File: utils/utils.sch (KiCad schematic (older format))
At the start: 20 parts, among them J1 AIN, J2 BIN, J3 GATE, J4 EURORACK_CONN_16, J5 ~OUT, J6 OUT, U1 TL072, U2 4066, U3 LM317L_TO92, U4 LM337L_TO92

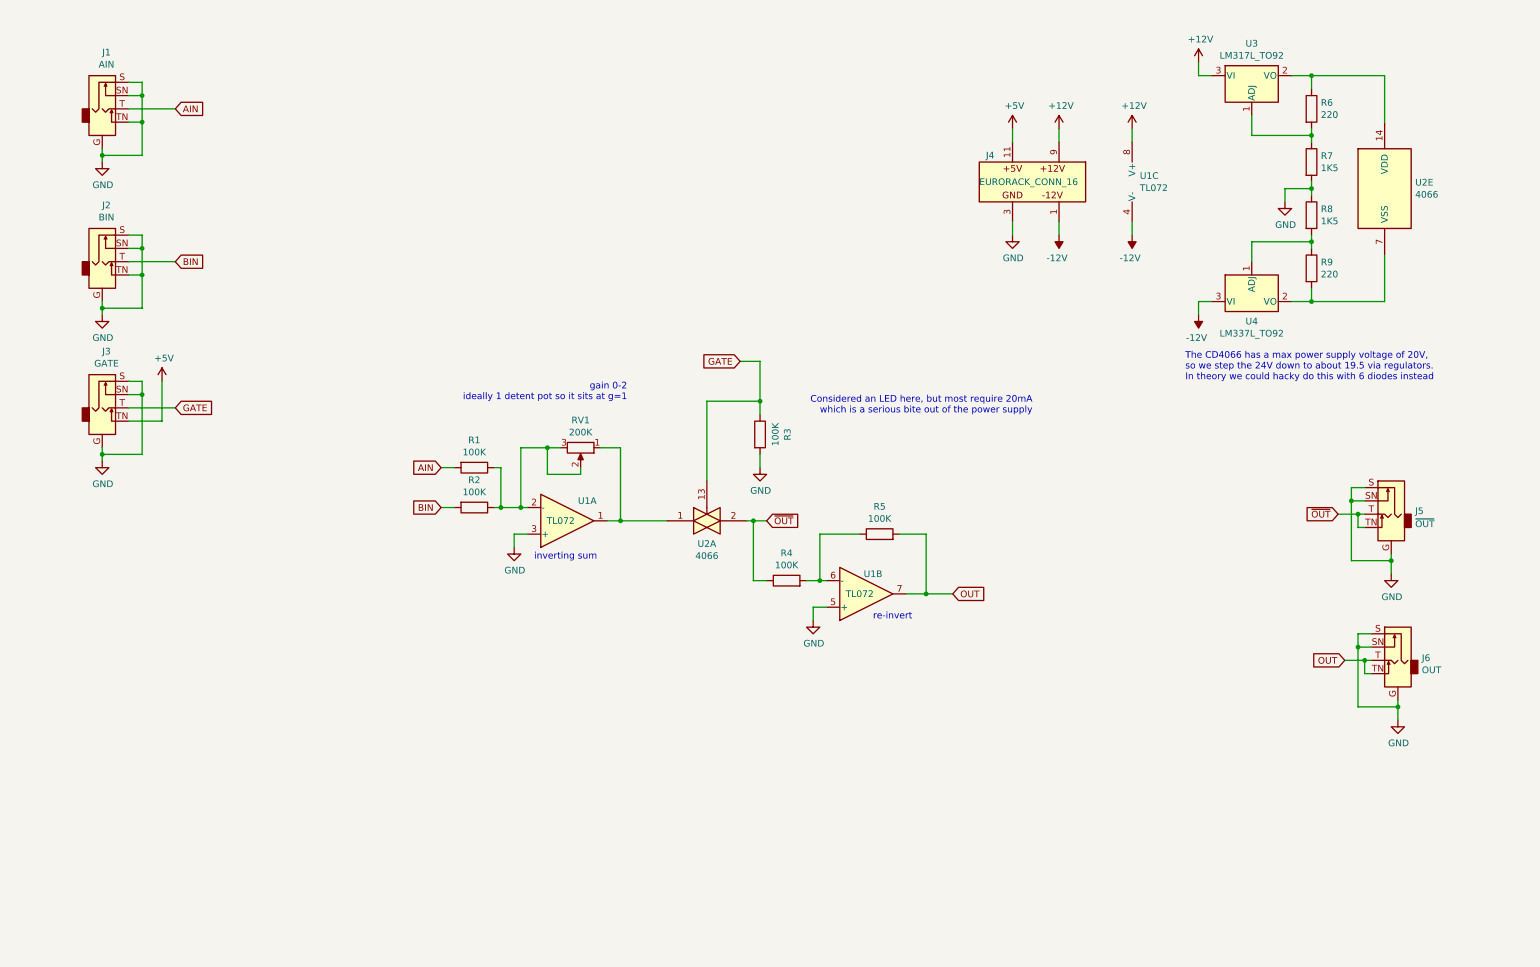
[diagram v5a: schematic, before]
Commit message: switch to 10-pin header
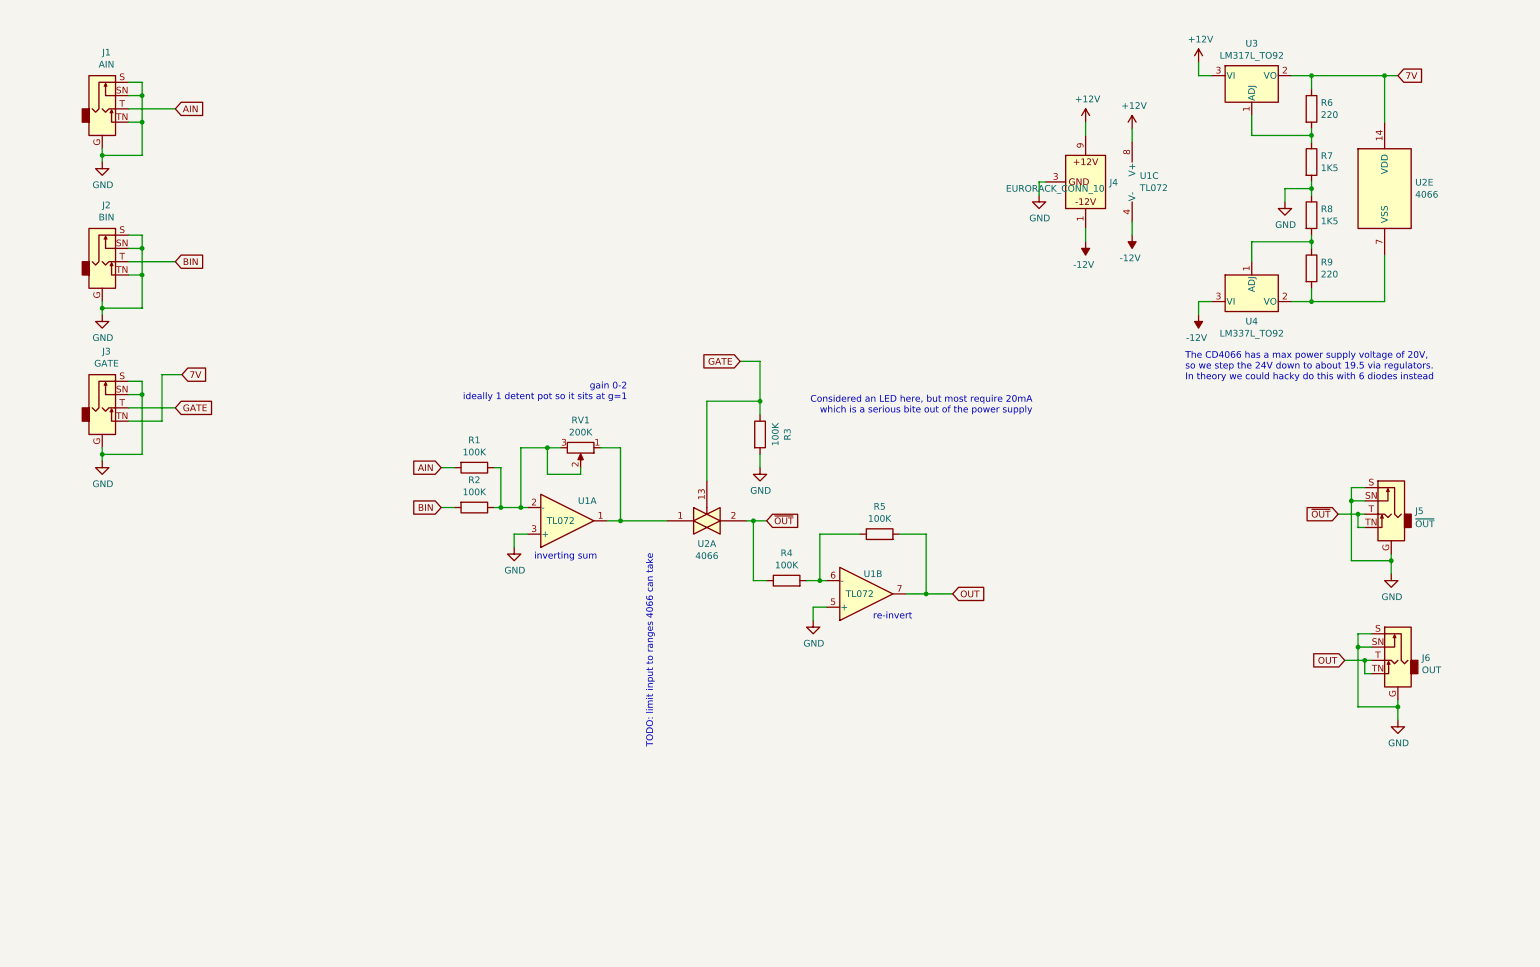
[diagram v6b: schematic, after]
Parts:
- removed J4: EURORACK_CONN_16, synth:EURORACK_16_IDC, symbol synth:EURORACK_CONN_16
- added J4: EURORACK_CONN_10, synth:EURORACK_10_IDC, symbol synth:EURORACK_CONN_10
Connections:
- net +5V is gone; now on net 7V: J3.TN
- net +12V: now also J4.9 (12V_P)
- net -12V: now also J4.1 (12V_N)
- net GND: now also J4.3 (GND)
- net 7V: now reaches R6.1, U2.14 (VDD), U3.2 (VO)
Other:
- note added: "TODO: limit input to ranges 4066 can take"
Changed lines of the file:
@@
 L power:+12V #PWR010
 U 1 1 5ECA049A
-P 8100 1300
-F 0 "#PWR010" H 8100 1150 50  0001 C CNN
-F 1 "+12V" H 8115 1473 50  0000 C CNN
-F 2 "" H 8100 1300 50  0001 C CNN
-F 3 "" H 8100 1300 50  0001 C CNN
-	1    8100 1300
+P 8300 1250
+F 0 "#PWR010" H 8300 1100 50  0001 C CNN
+F 1 "+12V" H 8315 1423 50  0000 C CNN
+F 2 "" H 8300 1250 50  0001 C CNN
+F 3 "" H 8300 1250 50  0001 C CNN
+	1    8300 1250
 	1    0    0    -1
 $EndComp
@@
 L power:-12V #PWR011
 U 1 1 5ECA0BEB
-P 8100 2100
-F 0 "#PWR011" H 8100 2200 50  0001 C CNN
-F 1 "-12V" H 8115 2273 50  0000 C CNN
-F 2 "" H 8100 2100 50  0001 C CNN
-F 3 "" H 8100 2100 50  0001 C CNN
-	1    8100 2100
+P 8300 2150
+F 0 "#PWR011" H 8300 2250 50  0001 C CNN
+F 1 "-12V" H 8315 2323 50  0000 C CNN
+F 2 "" H 8300 2150 50  0001 C CNN
+F 3 "" H 8300 2150 50  0001 C CNN
+	1    8300 2150
 	-1   0    0    1
 $EndComp
@@
 L power:GND #PWR09
 U 1 1 5ECA13B1
-P 7750 2100
-F 0 "#PWR09" H 7750 1850 50  0001 C CNN
-F 1 "GND" H 7755 1927 50  0000 C CNN
-F 2 "" H 7750 2100 50  0001 C CNN
-F 3 "" H 7750 2100 50  0001 C CNN
-	1    7750 2100
+P 7950 1800
+F 0 "#PWR09" H 7950 1550 50  0001 C CNN
+F 1 "GND" H 7955 1627 50  0000 C CNN
+F 2 "" H 7950 1800 50  0001 C CNN
+F 3 "" H 7950 1800 50  0001 C CNN
+	1    7950 1800
 	1    0    0    -1
 $EndComp
@@
 Wire Wire Line
 	1200 3300 1200 3750
-$Comp
-L power:+5V #PWR08
-U 1 1 5ECDDDF2
-P 7750 1300
-F 0 "#PWR08" H 7750 1150 50  0001 C CNN
-F 1 "+5V" H 7765 1473 50  0000 C CNN
-F 2 "" H 7750 1300 50  0001 C CNN
-F 3 "" H 7750 1300 50  0001 C CNN
-	1    7750 1300
-	1    0    0    -1
-$EndComp
-$Comp
-L power:+5V #PWR04
-U 1 1 5ECE0C8E
-P 1350 3200
-F 0 "#PWR04" H 1350 3050 50  0001 C CNN
-F 1 "+5V" H 1365 3373 50  0000 C CNN
-F 2 "" H 1350 3200 50  0001 C CNN
-F 3 "" H 1350 3200 50  0001 C CNN
-	1    1350 3200
-	1    0    0    -1
-$EndComp
-Wire Wire Line
-	1350 3200 1350 3500
 Wire Wire Line
 	1350 3500 1100 3500
@@
 Text Notes 6700 5000 0    50   ~ 0
 re-invert
-$Comp
-L synth:EURORACK_CONN_16 J4
-U 1 1 5EC9CC05
-P 8150 1650
-F 0 "J4" H 7550 1800 50  0000 L CNN
-F 1 "EURORACK_CONN_16" H 7500 1600 50  0000 L CNN
-F 2 "synth:EURORACK_16_IDC" V 8200 1700 50  0001 C CNN
-F 3 "https://division-6.com/learn/eurorack-power/" V 8200 1700 50  0001 C CNN
-	1    8150 1650
-	1    0    0    -1
-$EndComp
 Wire Wire Line
 	10400 4300 10350 4300
@@
 Wire Wire Line
 	8650 2100 8650 2000
-Wire Wire Line
-	8100 1300 8100 1400
-Wire Wire Line
-	8100 2100 8100 2000
-Wire Wire Line
-	7750 2100 7750 2000
-Wire Wire Line
-	7750 1300 7750 1400
 $Comp
 L Amplifier_Operational:TL072 U1
@@
 Wire Wire Line
 	10550 1250 10550 900
-Wire Wire Line
-	10550 900  10000 900
 Connection ~ 10000 900
 Wire Wire Line
@@
 Wire Wire Line
 	4800 4250 5150 4250
+$Comp
+L synth:EURORACK_CONN_10 J4
+U 1 1 5ED02358
+P 8300 1700
+F 0 "J4" H 8480 1696 50  0000 L CNN
+F 1 "EURORACK_CONN_10" H 7700 1650 50  0000 L CNN
+F 2 "synth:EURORACK_10_IDC" H 7500 1450 50  0001 C CNN
+F 3 "https://division-6.com/learn/eurorack-power/" V 8350 1750 50  0001 C CNN
+	1    8300 1700
+	1    0    0    -1
+$EndComp
+Text Notes 5050 4500 3    50   ~ 0
+TODO: limit input to ranges 4066 can take
+Wire Wire Line
+	7950 1800 7950 1700
+Wire Wire Line
+	7950 1700 8000 1700
+Wire Wire Line
+	8300 2150 8300 2050
+Wire Wire Line
+	8300 1350 8300 1250
+Text GLabel 10650 900  2    50   Input ~ 0
+7V
+Wire Wire Line
+	10000 900  10550 900
+Connection ~ 10550 900
+Wire Wire Line
+	10550 900  10650 900
+Text GLabel 1500 3150 2    50   Input ~ 0
+7V
+Wire Wire Line
+	1500 3150 1350 3150
+Wire Wire Line
+	1350 3150 1350 3500
 $EndSCHEMATC

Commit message: use +/-10V power supply for amps
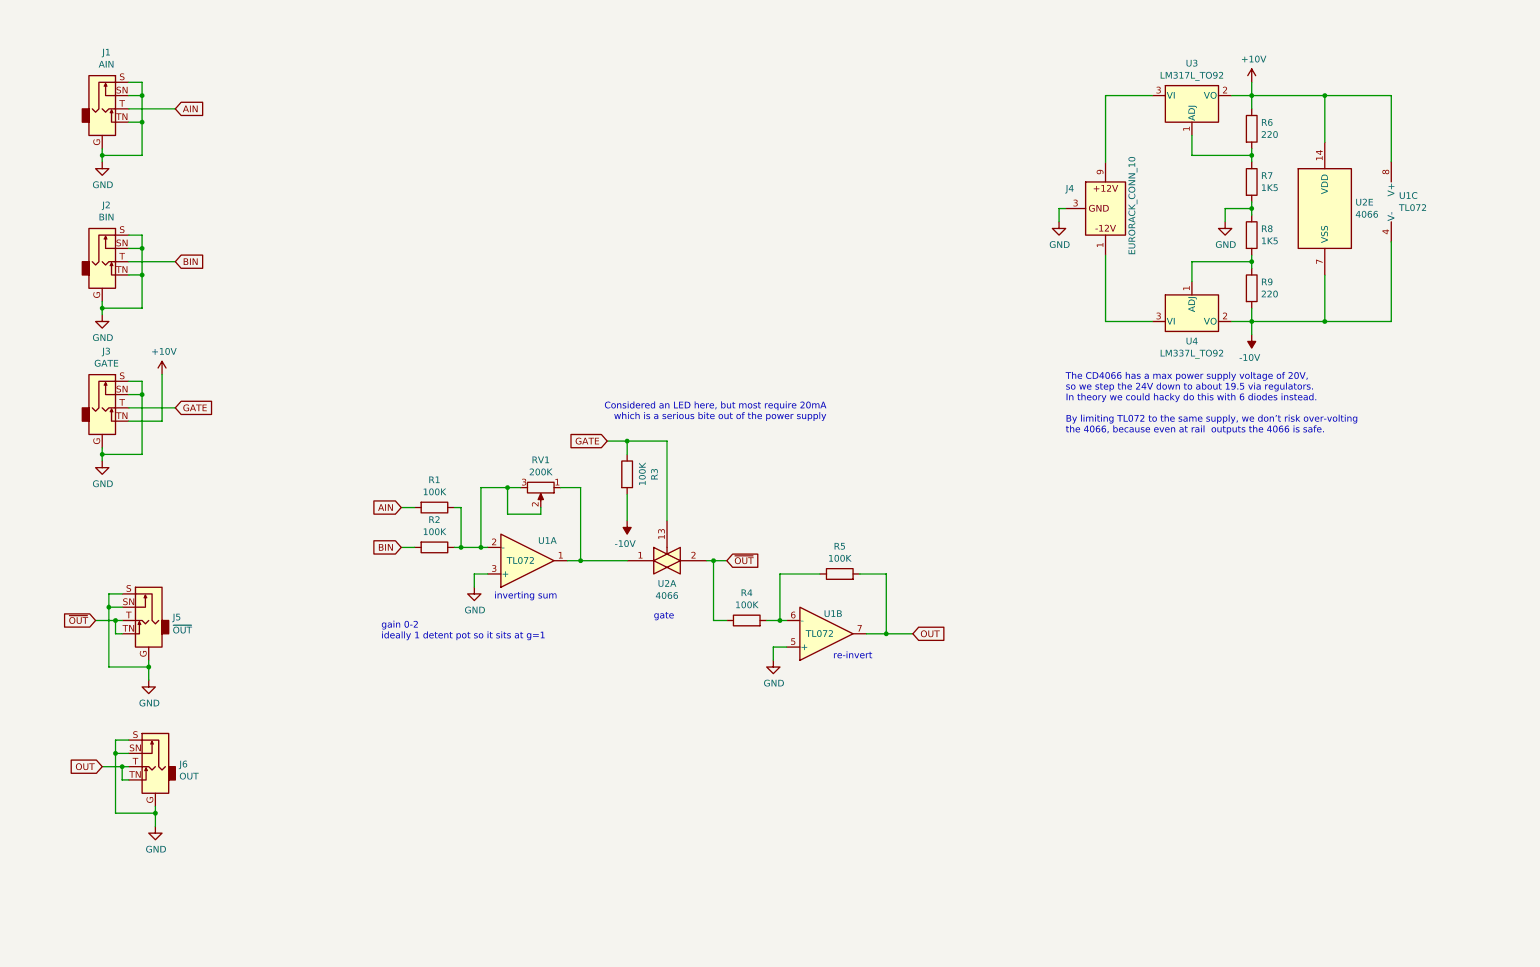
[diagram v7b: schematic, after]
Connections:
- net GND: no longer R3.2
- net -10V: now reaches R9.2, U2.7 (VSS), U4.2 (VO)
- net -10V: now also R3.2, U1.4 (V-)
- net +12V: no longer names the net of J4.9 (12V_P), U3.3 (VI)
- net +12V: no longer U1.8 (V+)
- net -12V: no longer names the net of J4.1 (12V_N), U4.3 (VI)
- net -12V: no longer U1.4 (V-)
- net 7V renamed +10V
- net +10V: now also U1.8 (V+)
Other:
- note added: "The CD4066 has a max power supply voltage of 20V,\nso we step the 24V down to about 19.5 via regulators.\nIn theory we could hacky do this with 6 diodes instead.\n\nBy limiting TL072 to the same supply, we don’t risk over-volting\nthe 4066, because even at rail outputs the 4066 is safe."
- note added: "gate"
- note removed: "TODO: limit input to ranges 4066 can take"
- note removed: "The CD4066 has a max power supply voltage of 20V,\nso we step the 24V down to about 19.5 via regulators.\nIn theory we could hacky do this with 6 diodes instead"
- moved on the sheet: J4, J5, J6, R1, R2, R3, R4, R5, R6, R7, R8, R9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

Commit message: reconnect 4066 headers
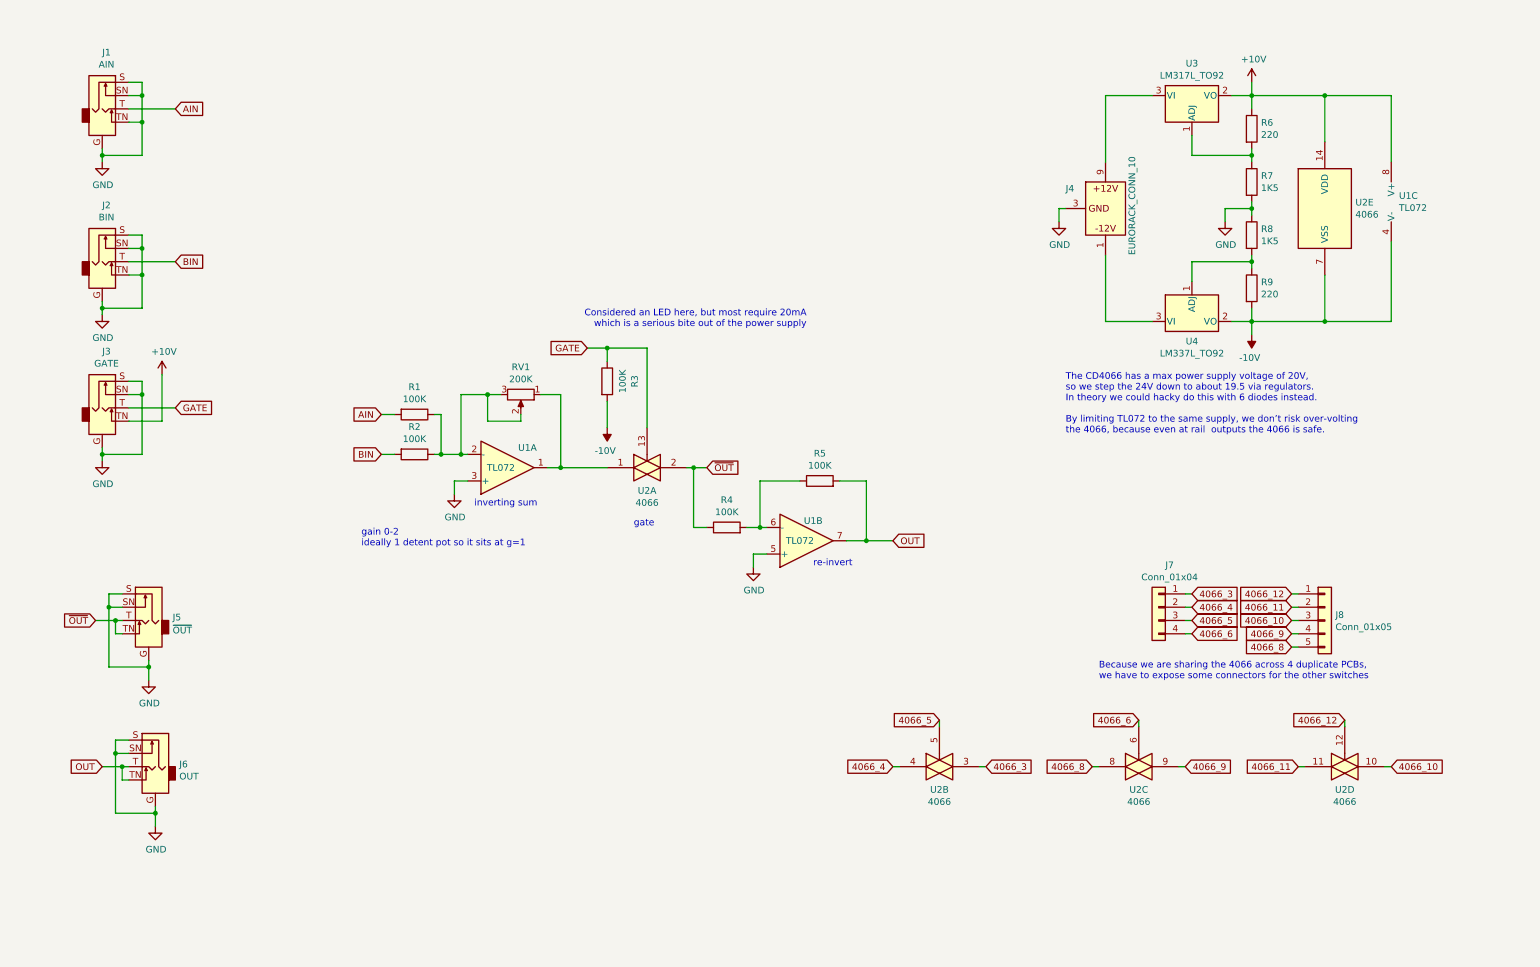
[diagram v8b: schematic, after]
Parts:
- added J7: Conn_01x04, imciner2/KiCad-Libraries/modules/Connectors.pretty:CONN_2.54mm_1x04, symbol Connector_Generic:Conn_01x04
- added J8: Conn_01x05, imciner2/KiCad-Libraries/modules/Connectors.pretty:CONN_2.54mm_1x05, symbol Connector_Generic:Conn_01x05
- added unit 2 of U2
- added unit 3 of U2
- added unit 4 of U2
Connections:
- new net 4066_10: J8.3 (Pin_3), U2.10
- new net 4066_11: J8.2 (Pin_2), U2.11
- new net 4066_12: J8.1 (Pin_1), U2.12
- new net 4066_3: J7.1 (Pin_1), U2.3
- new net 4066_4: J7.2 (Pin_2), U2.4
- new net 4066_5: J7.3 (Pin_3), U2.5
- new net 4066_6: J7.4 (Pin_4), U2.6
- new net 4066_8: J8.5 (Pin_5), U2.8
- new net 4066_9: J8.4 (Pin_4), U2.9
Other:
- note added: "Because we are sharing the 4066 across 4 duplicate PCBs,\nwe have to expose some connectors for the other switches"
- moved on the sheet: R1, R2, R3, R4, R5, RV1, U1A, U1B, U2A
